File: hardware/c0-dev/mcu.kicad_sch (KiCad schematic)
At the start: 52 parts, among them J401 TAG_CONNECT, J402 PinHeader_2.54mm, U401 TCA9555PWR, U402 W25Q128JVP, U403 RP2350A, U404 TPS3820-33DBV, Y401 ABM8-272-T3 (12Mhz)

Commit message: inital placement done
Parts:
- J402: footprint Connector_PinHeader_2.54mm:PinHeader_1x03_P2.54mm_Vertical_SMD_Pin1Left -> Connector_PinHeader_2.54mm:PinHeader_1x03_P2.54mm_Vertical
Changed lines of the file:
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@@
 			)
 		)
-		(property "Footprint" "Connector_PinHeader_2.54mm:PinHeader_1x03_P2.54mm_Vertical_SMD_Pin1Left"
+		(property "Footprint" "Connector_PinHeader_2.54mm:PinHeader_1x03_P2.54mm_Vertical"
 			(at 152.4 135.89 0)
 			(hide yes)

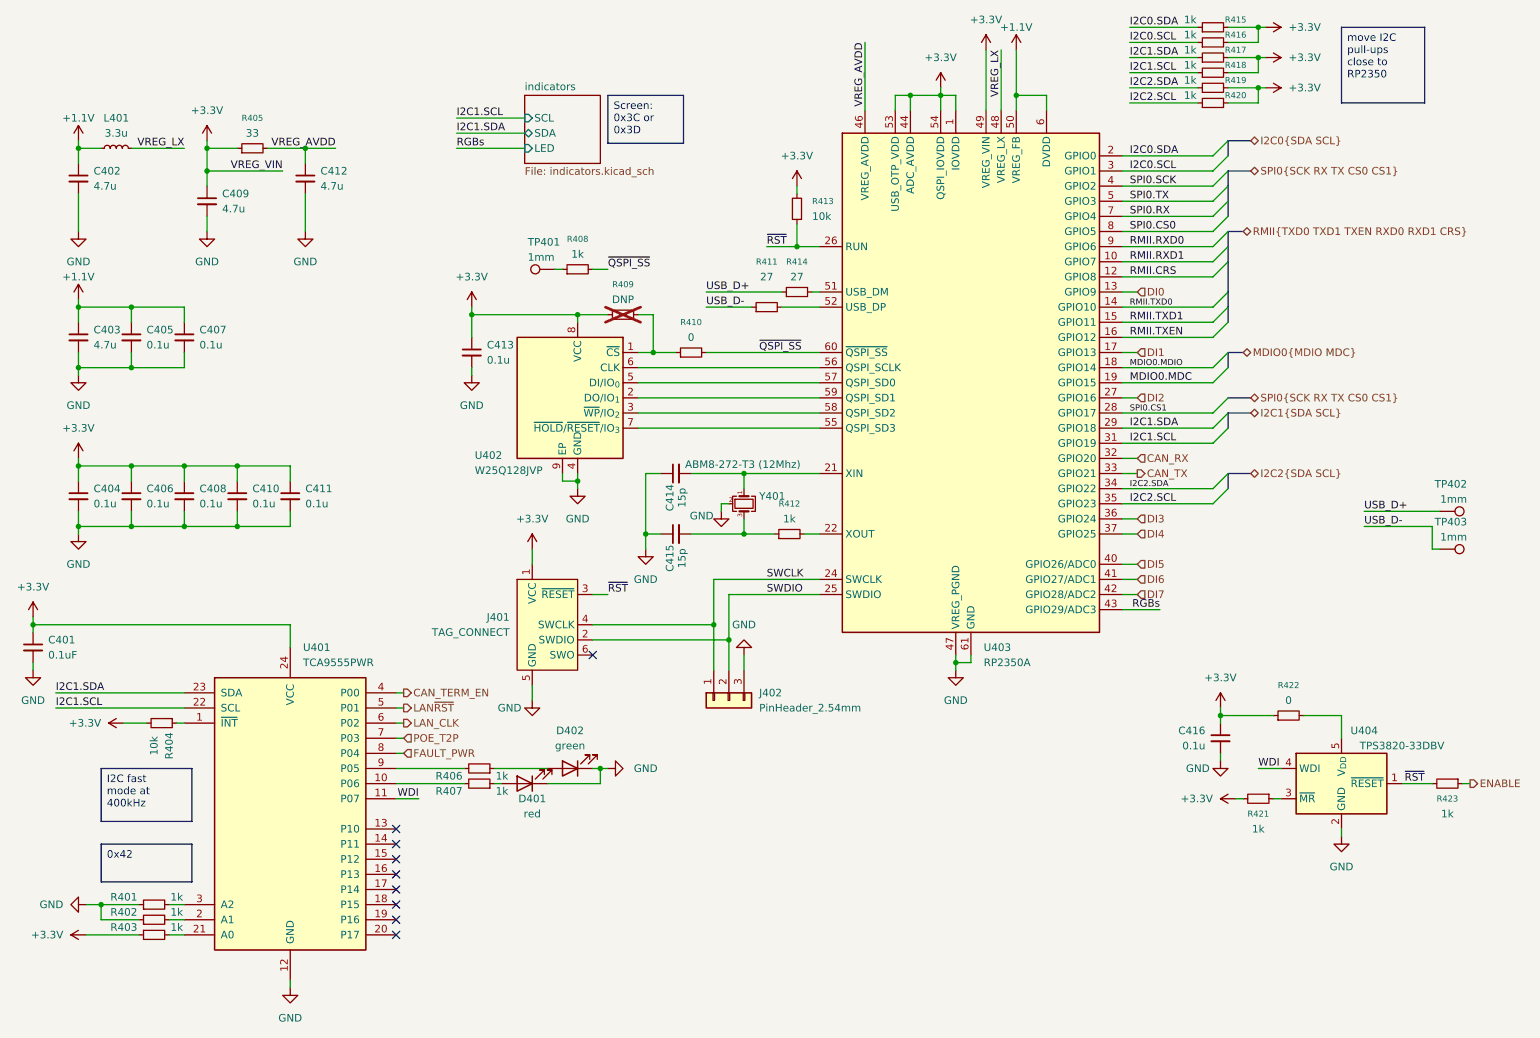
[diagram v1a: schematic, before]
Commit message: silkscreen, isolation and placement cleanup
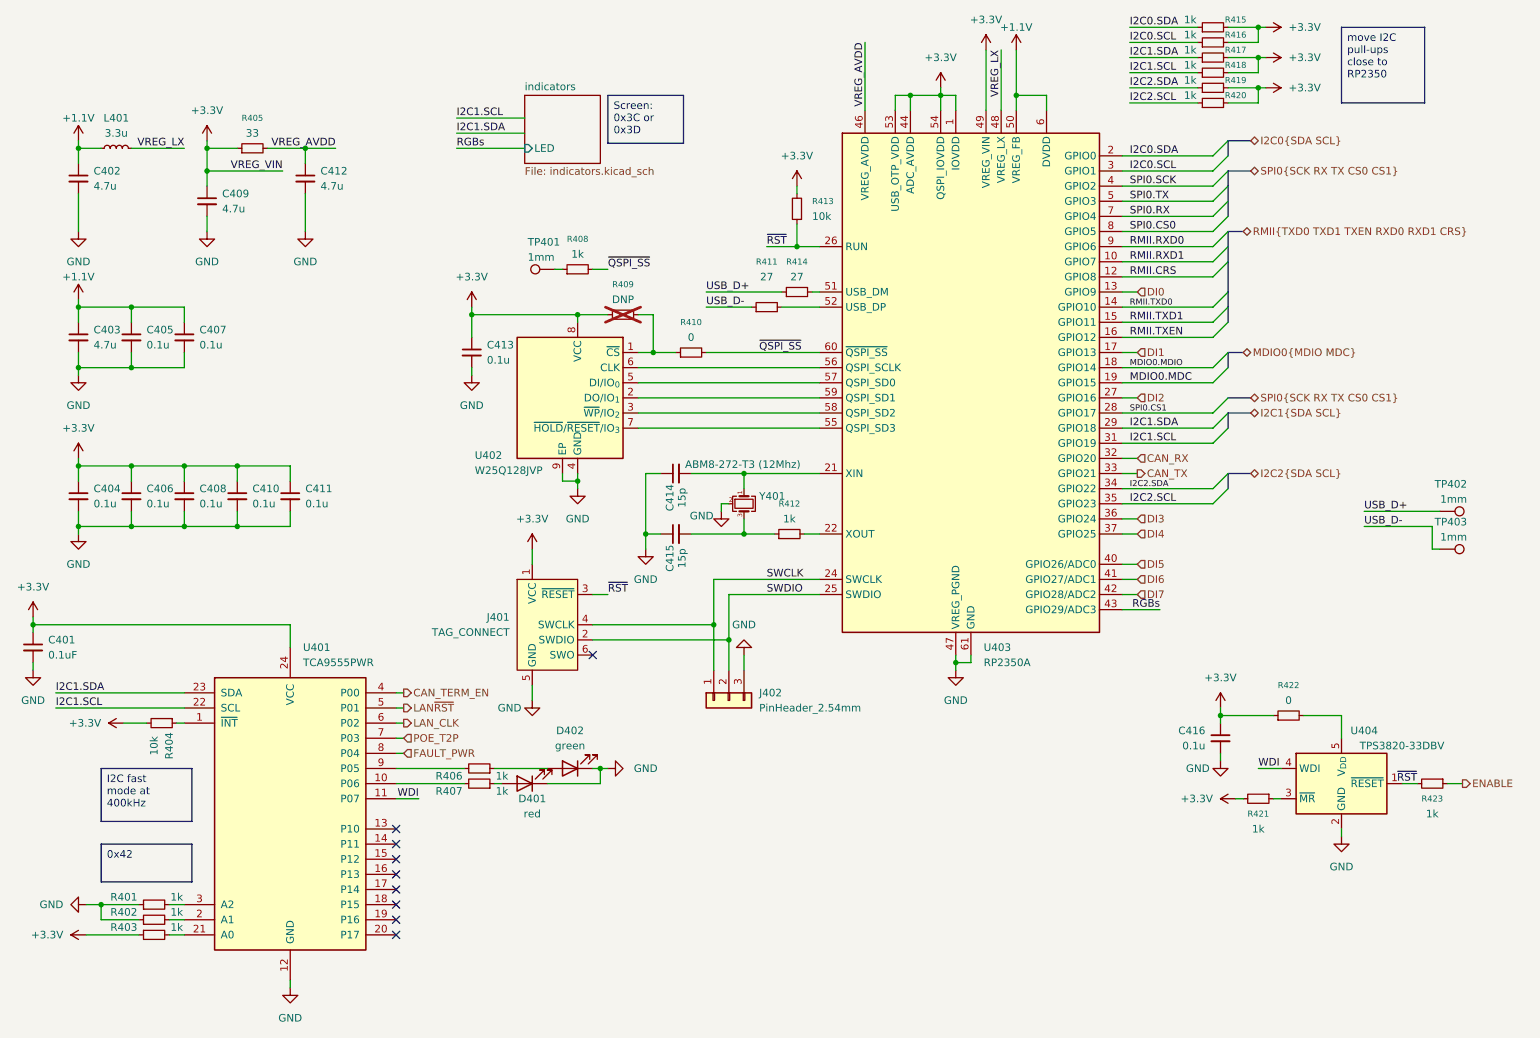
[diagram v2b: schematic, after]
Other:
- sheet indicators ports: added none; removed SCL, SDA
- moved on the sheet: R423
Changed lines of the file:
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@@
 	(wire
 		(pts
+			(xy 265.43 149.86) (xy 267.97 149.86)
+		)
+		(stroke
+			(width 0)
+			(type default)
+		)
+	)
+	(wire
+		(pts
 			(xy 218.44 57.15) (xy 233.68 57.15)
 		)
@@
 	(wire
 		(pts
-			(xy 275.59 149.86) (xy 276.86 149.86)
+			(xy 273.05 149.86) (xy 275.59 149.86)
 		)
 		(stroke
@@
 	(wire
 		(pts
-			(xy 265.43 149.86) (xy 270.51 149.86)
-		)
-		(stroke
-			(width 0)
-			(type default)
-		)
-	)
-	(wire
-		(pts
 			(xy 241.3 27.94) (xy 242.57 27.94)
 		)
@@
 	)
 	(label "~{RST}"
-		(at 269.24 149.86 180)
+		(at 267.97 149.86 180)
 		(effects
 			(font
@@
 	(hierarchical_label "ENABLE"
 		(shape output)
-		(at 276.86 149.86 0)
+		(at 275.59 149.86 0)
 		(effects
 			(font
@@
 	(symbol
 		(lib_id "Device:R_Small")
-		(at 273.05 149.86 270)
+		(at 270.51 149.86 270)
 		(unit 1)
 		(body_style 1)
@@
 		(dnp no)
 		(property "Reference" "R423"
-			(at 273.05 152.4 90)
+			(at 270.51 152.4 90)
 			(show_name no)
 			(do_not_autoplace no)
@@
 		)
 		(property "Value" "1k"
-			(at 273.05 154.94 90)
+			(at 270.51 154.94 90)
 			(show_name no)
 			(do_not_autoplace no)
@@
 		)
 		(property "Footprint" "Resistor_SMD:R_0402_1005Metric"
-			(at 273.05 149.86 0)
+			(at 270.51 149.86 0)
 			(hide yes)
 			(show_name no)
@@
 		)
 		(property "Datasheet" ""
-			(at 273.05 149.86 0)
+			(at 270.51 149.86 0)
 			(hide yes)
 			(show_name no)
@@
 		)
 		(property "Description" "Resistor, small symbol"
-			(at 273.05 149.86 0)
+			(at 270.51 149.86 0)
 			(hide yes)
 			(show_name no)
@@
 			)
 		)
-		(pin "SCL" input
-			(at 118.11 38.1 180)
-			(effects
-				(font
-					(size 1.27 1.27)
-				)
-				(justify left)
-			)
-		)
-		(pin "SDA" bidirectional
-			(at 118.11 40.64 180)
-			(effects
-				(font
-					(size 1.27 1.27)
-				)
-				(justify left)
-			)
-		)

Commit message: added 3d models
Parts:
- U403: footprint Package_DFN_QFN:QFN-60-1EP_7x7mm_P0.4mm_EP3.4x3.4mm -> conduit:QFN-60-1EP_7x7mm_P0.4mm_EP3.4x3.4mm
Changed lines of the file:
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@@
 			)
 		)
-		(property "Footprint" "Package_DFN_QFN:QFN-60-1EP_7x7mm_P0.4mm_EP3.4x3.4mm"
+		(property "Footprint" "conduit:QFN-60-1EP_7x7mm_P0.4mm_EP3.4x3.4mm"
 			(at 193.04 82.55 0)
 			(hide yes)
